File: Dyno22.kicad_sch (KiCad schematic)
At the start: 35 parts, among them J1 Screen_Left, J2 Screen_Right, J3 Pwr Input, J4 I2C, J5 Pwr Output, SW1 Rotary Encoder, U1 LM324

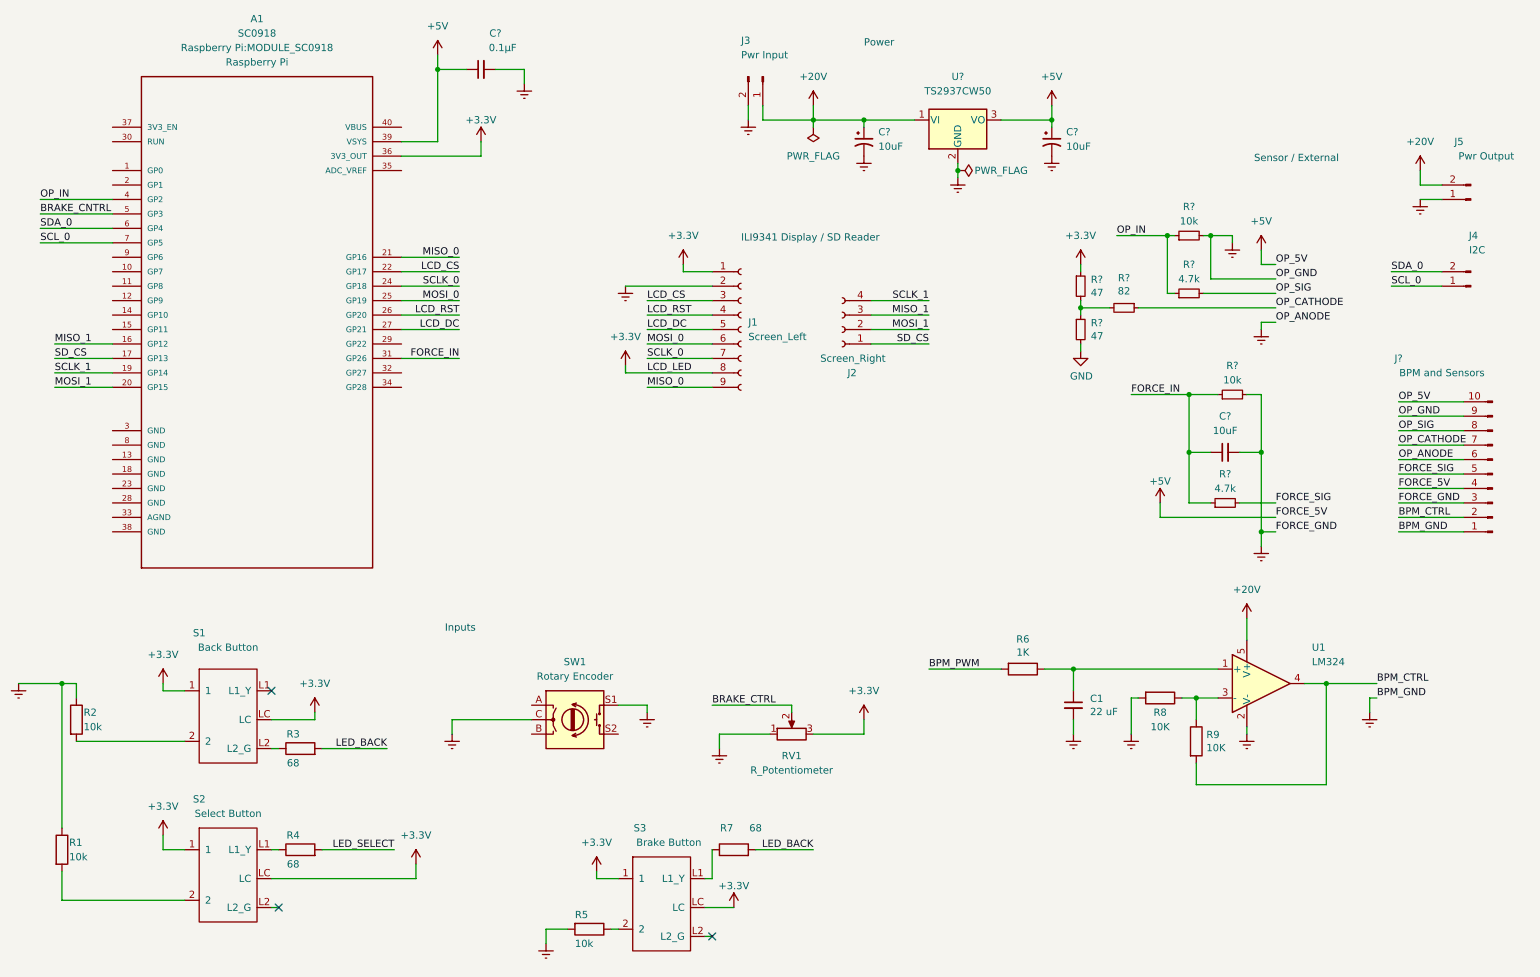
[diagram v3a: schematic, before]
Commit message: Adds connections for all button pins
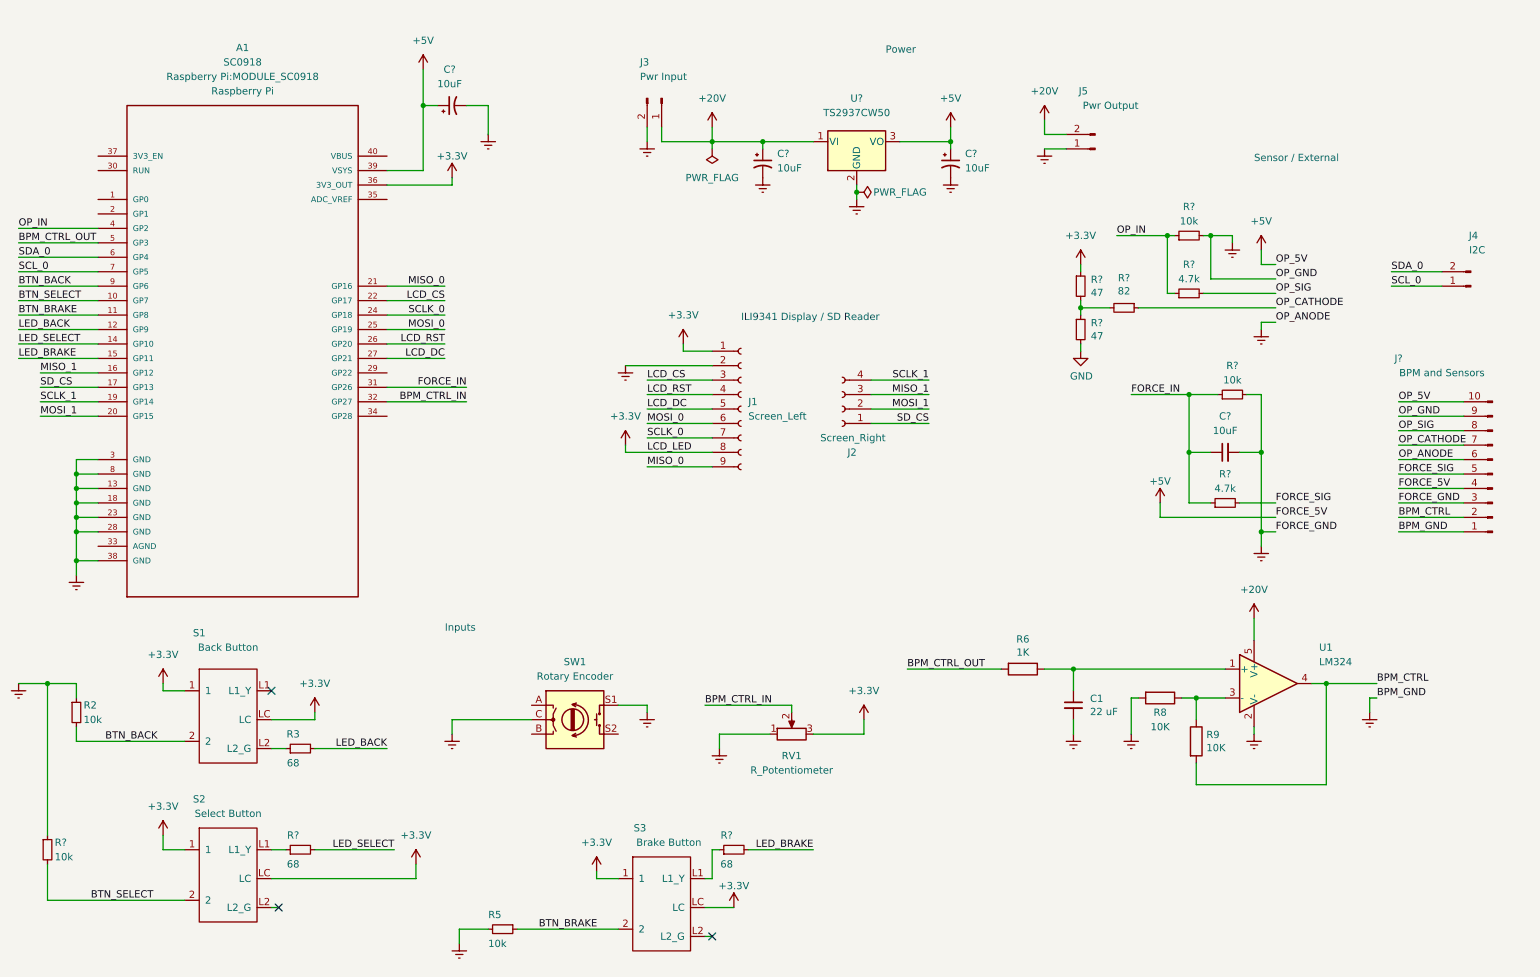
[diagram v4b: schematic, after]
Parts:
- removed C?: 0.1µF, symbol Device:C_Small
- removed R1: 10k, Resistor_SMD:R_0805_2012Metric, symbol Device:R
- removed R4, R7: 68, Resistor_SMD:R_0805_2012Metric, symbol Device:R
- added C?: 10uF, symbol Device:C_Polarized_Small_US
- added R? (x2): 68, Resistor_SMD:R_0805_2012Metric, symbol Device:R_Small
- added R?: 10k, Resistor_SMD:R_0805_2012Metric, symbol Device:R_Small
- R2, R3, R5: symbol Device:R -> Device:R_Small
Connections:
- net BRAKE_CNTRL is gone; now on net BPM_CTRL_OUT: A1.5 (GP3)
- net BRAKE_CTRL is gone; now on net BPM_CTRL_IN: RV1.2
- net +5V: now also C?.1
- net Earth: now also A1.13 (GND), A1.18 (GND), A1.23 (GND), A1.28 (GND), A1.3 (GND), A1.38 (GND), A1.8 (GND), C?.2, R?.1
- net LED_BACK: now also A1.12 (GP9)
- net LED_SELECT: now also A1.14 (GP10), R?.2
- net BTN_BRAKE: now reaches R5.1, S3.2
- net BTN_BRAKE: now also A1.11 (GP8)
- net at S3.L1 (L1_Y): now also R?.1
- net BTN_SELECT: now reaches A1.10 (GP7)
- net BTN_SELECT: now also S2.2, R?.2
- net LED_BRAKE: now reaches A1.15 (GP11)
- net LED_BRAKE: now also R?.2
- net BPM_CTRL_IN: now reaches A1.32 (GP27)
- net BTN_BACK: now reaches A1.9 (GP6)
- net BTN_BACK: now also R2.2, S1.2
- net at S2.L1 (L1_Y): now also R?.1
- net BPM_PWM renamed BPM_CTRL_OUT
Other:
- moved on the sheet: A1, C?, J1, J2, J3, J5, R2, R5, U1, U?

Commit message: Fixes pin headers for lcd display
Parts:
- J3: renamed from J2; symbol Connector:Conn_01x04_Female -> Connector:Conn_01x05_Female
- R11: renamed from R8; symbol Device:R -> Device:R_Small
- R14: renamed from R9; symbol Device:R -> Device:R_Small
- R7: renamed from R6; symbol Device:R -> Device:R_Small
- gave numbers to parts that had none: 16
- renumbered C1 to C4, J3 to J1, J1 to J2, J5 to J4, J4 to J5, U1 to U2
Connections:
- net UART_RX: now reaches A1.30 (RUN)
- net UART_TX: now reaches A1.37 (3V3_EN)
- no-connect marks 3 -> 4
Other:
- moved on the sheet: R10, R5, R6, S3

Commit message: Modifies op amp circuit -- 3.3V -> 10V pwm
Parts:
- R11: value 10K -> 5k
- R14: value 10K -> 10k
- R7: value 1K -> 1k
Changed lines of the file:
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@@
   (junction (at 140.97 35.56) (diameter 0) (color 0 0 0 0)
   )
-  (junction (at 248.92 130.81) (diameter 0) (color 0 0 0 0)
-  )
   (junction (at 182.88 35.56) (diameter 0) (color 0 0 0 0)
   )
@@
   )
   (junction (at 228.6 52.07) (diameter 0) (color 0 0 0 0)
+  )
+  (junction (at 247.65 130.81) (diameter 0) (color 0 0 0 0)
   )
   (no_connect (at 63.5 132.08))
@@
     (stroke (width 0) (type default) (color 0 0 0 0))
   )
-  (wire (pts (xy 248.92 148.59) (xy 248.92 130.81))
+  (wire (pts (xy 247.65 148.59) (xy 247.65 130.81))
     (stroke (width 0) (type default) (color 0 0 0 0))
   )
@@
     (stroke (width 0) (type default) (color 0 0 0 0))
   )
-  (wire (pts (xy 248.92 130.81) (xy 257.81 130.81))
+  (wire (pts (xy 247.65 130.81) (xy 257.81 130.81))
     (stroke (width 0) (type default) (color 0 0 0 0))
   )
@@
     (stroke (width 0) (type default) (color 0 0 0 0))
   )
-  (wire (pts (xy 226.06 148.59) (xy 248.92 148.59))
+  (wire (pts (xy 226.06 148.59) (xy 247.65 148.59))
     (stroke (width 0) (type default) (color 0 0 0 0))
   )
@@
     (stroke (width 0) (type default) (color 0 0 0 0))
   )
-  (wire (pts (xy 246.38 130.81) (xy 248.92 130.81))
+  (wire (pts (xy 246.38 130.81) (xy 247.65 130.81))
     (stroke (width 0) (type default) (color 0 0 0 0))
   )
@@
     (in_bom yes) (on_board yes)
     (property "Reference" "R7" (id 0) (at 195.58 123.0122 90))
-    (property "Value" "1K" (id 1) (at 195.58 125.3236 90))
+    (property "Value" "1k" (id 1) (at 195.58 125.3236 90))
     (property "Footprint" "Resistor_SMD:R_0805_2012Metric_Pad1.20x1.40mm_HandSolder" (id 2) (at 195.58 128.27 0)
       (effects (font (size 1.27 1.27)) hide)
@@
       (effects (font (size 1.27 1.27)) (justify left))
     )
-    (property "Value" "10K" (id 1) (at 227.838 142.113 0)
+    (property "Value" "10k" (id 1) (at 227.838 142.113 0)
       (effects (font (size 1.27 1.27)) (justify left))
     )
@@
     (in_bom yes) (on_board yes)
     (property "Reference" "R11" (id 0) (at 219.71 135.89 90))
-    (property "Value" "10K" (id 1) (at 219.71 138.43 90))
+    (property "Value" "5k" (id 1) (at 219.71 138.43 90))
     (property "Footprint" "Resistor_SMD:R_0805_2012Metric_Pad1.20x1.40mm_HandSolder" (id 2) (at 219.71 133.35 0)
       (effects (font (size 1.27 1.27)) hide)
@@
     )
     (path "/00000000-0000-0000-0000-0000635e1f65"
-      (reference "R7") (unit 1) (value "1K") (footprint "Resistor_SMD:R_0805_2012Metric_Pad1.20x1.40mm_HandSolder")
+      (reference "R7") (unit 1) (value "1k") (footprint "Resistor_SMD:R_0805_2012Metric_Pad1.20x1.40mm_HandSolder")
     )
     (path "/6d09b5fa-6a8e-4172-a969-7a991ead894c"
@@
     )
     (path "/00000000-0000-0000-0000-0000635e59c1"
-      (reference "R11") (unit 1) (value "10K") (footprint "Resistor_SMD:R_0805_2012Metric_Pad1.20x1.40mm_HandSolder")
+      (reference "R11") (unit 1) (value "5k") (footprint "Resistor_SMD:R_0805_2012Metric_Pad1.20x1.40mm_HandSolder")
     )
     (path "/f53c7d96-56fb-461a-9a22-e54c8ae4ab26"
@@
     )
     (path "/00000000-0000-0000-0000-0000635e48e5"
-      (reference "R14") (unit 1) (value "10K") (footprint "Resistor_SMD:R_0805_2012Metric_Pad1.20x1.40mm_HandSolder")
+      (reference "R14") (unit 1) (value "10k") (footprint "Resistor_SMD:R_0805_2012Metric_Pad1.20x1.40mm_HandSolder")
     )
     (path "/ab9db61d-8817-4ba4-abb7-6f3dccbf68b1"

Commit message: uart labels assigned to wrong pins
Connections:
- net UART_RX: now also A1.2 (GP1); no longer A1.30 (RUN)
- net UART_TX: now also A1.1 (GP0); no longer A1.37 (3V3_EN)
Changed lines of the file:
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@@
-    (stroke (width 0) (type default) (color 0 0 0 0))
-  )
-  (wire (pts (xy 24.13 38.1) (xy 33.02 38.1))
     (stroke (width 0) (type default) (color 0 0 0 0))
   )
@@
     (stroke (width 0) (type default) (color 0 0 0 0))
   )
-  (wire (pts (xy 24.13 40.64) (xy 33.02 40.64))
-    (stroke (width 0) (type default) (color 0 0 0 0))
-  )
   (wire (pts (xy 83.82 73.66) (xy 93.98 73.66))
     (stroke (width 0) (type default) (color 0 0 0 0))
@@
     (effects (font (size 1.27 1.27)) (justify left bottom))
   )
+  (label "UART_RX" (at 19.05 48.26 0)
+    (effects (font (size 1.27 1.27)) (justify left bottom))
+  )
   (label "OP_5V" (at 261.62 81.28 0)
     (effects (font (size 1.27 1.27)) (justify left bottom))
@@
     (effects (font (size 1.27 1.27)) (justify left bottom))
   )
-  (label "UART_RX" (at 24.13 40.64 0)
-    (effects (font (size 1.27 1.27)) (justify left bottom))
-  )
   (label "FORCE_GND" (at 261.62 99.06 0)
-    (effects (font (size 1.27 1.27)) (justify left bottom))
-  )
-  (label "UART_TX" (at 24.13 38.1 0)
     (effects (font (size 1.27 1.27)) (justify left bottom))
   )
@@
     (effects (font (size 1.27 1.27)) (justify left bottom))
   )
+  (label "UART_TX" (at 19.05 45.72 0)
+    (effects (font (size 1.27 1.27)) (justify left bottom))
+  )

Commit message: Adds graphics to pcb
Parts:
- removed J2: Screen_Left, symbol Connector:Conn_01x09_Female
- removed J3: Screen_Right, Connector_PinHeader_2.54mm:PinHeader_1x04_P2.54mm_Vertical, symbol Connector:Conn_01x05_Female
- added H1, H2, H3, H4: MountingHole, MountingHole:MountingHole_3.2mm_M3, symbol Mechanical:MountingHole
- added J2: Display, custom_connectors:ILI9351_Large_Display, symbol Connector_Generic:Conn_02x09_Top_Bottom
- A1: value SC0918 -> PICO W; footprint Raspberry Pi:MODULE_SC0918 -> Raspberry_Pi_Pico_W_Kicad_Files-main:MODULE_SC0918
- C1, C2, C3: footprint (none) -> Capacitor_SMD:C_1206_3216Metric
- C4: footprint Capacitor_SMD:C_0805_2012Metric_Pad1.18x1.45mm_HandSolder -> Capacitor_SMD:C_0805_2012Metric
- C5: footprint (none) -> Capacitor_SMD:C_0805_2012Metric
- J4: renamed from J5; footprint Connector_Molex:Molex_Nano-Fit_105313-xx02_1x02_P2.50mm_Horizontal -> custom_connectors:Molex-70551-0036-MFG
- J5: renamed from J6; footprint (none) -> custom_connectors:Molex_Connector_SL_01x10_Header_Horizontal
- R10, R11, R14, R7, R8, R9: footprint Resistor_SMD:R_0805_2012Metric_Pad1.20x1.40mm_HandSolder -> Resistor_SMD:R_0805_2012Metric
- R12, R13, R15, R16: footprint (none) -> Resistor_SMD:R_0805_2012Metric
- renumbered J4 to J3
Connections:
- net +24V: now also J1.2 (Pin_2); no longer J1.1 (Pin_1)
- net +3.3V: now also J2.1 (Pin_1), J2.8 (Pin_8)
- net BTN_BRAKE: now also A1.14 (GP10); no longer A1.11 (GP8)
- net BTN_SELECT: now also A1.11 (GP8); no longer A1.10 (GP7)
- net Earth: now also J1.1 (Pin_1), J2.2 (Pin_2); no longer J1.2 (Pin_2)
- net LCD_CS: now also J2.3 (Pin_3)
- net LCD_DC: now also J2.5 (Pin_5)
- net LCD_RST: now also J2.4 (Pin_4)
- net LED_BACK: now also A1.10 (GP7); no longer A1.12 (GP9)
- net LED_SELECT: now also A1.12 (GP9); no longer A1.14 (GP10)
- net MISO_0: now also J2.9 (Pin_9)
- net MISO_1: now also J2.17 (Pin_17)
- net MOSI_0: now also J2.6 (Pin_6)
- net MOSI_1: now also J2.16 (Pin_16)
- net SCLK_0: now also J2.7 (Pin_7)
- net SCLK_1: now also J2.18 (Pin_18)
- net SCL_0: now also J4.2 (Pin_2); no longer J4.1 (Pin_1)
- net SDA_0: now also J4.1 (Pin_1); no longer J4.2 (Pin_2)
- net SD_CS: now also J2.15 (Pin_15)
- no-connect marks 4 -> 8
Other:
- moved on the sheet: J1, J3, J4
